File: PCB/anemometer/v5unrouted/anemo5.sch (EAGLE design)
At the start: 77 parts, among them IC1 AD8223, IC2 AD8223, IC3 AD8223, IC4 AD8223, IC5 TL072D, IC6 TL072D, IC7 TL072D, J1 RJ12STRAIGHT-I2C, J2 RJ12STRAIGHT-I2C

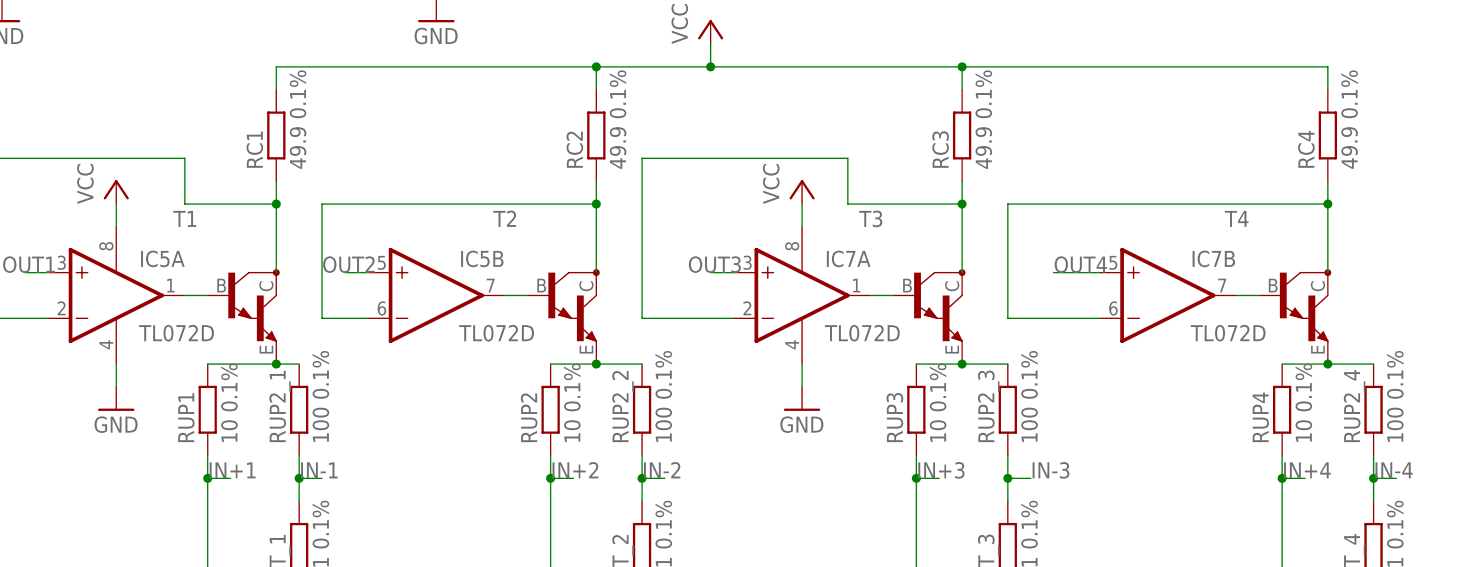
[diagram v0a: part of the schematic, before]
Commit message: changet to PNP darlington in unrouted anemometer file. should be rerouted if needed! (no changes in routed files...)
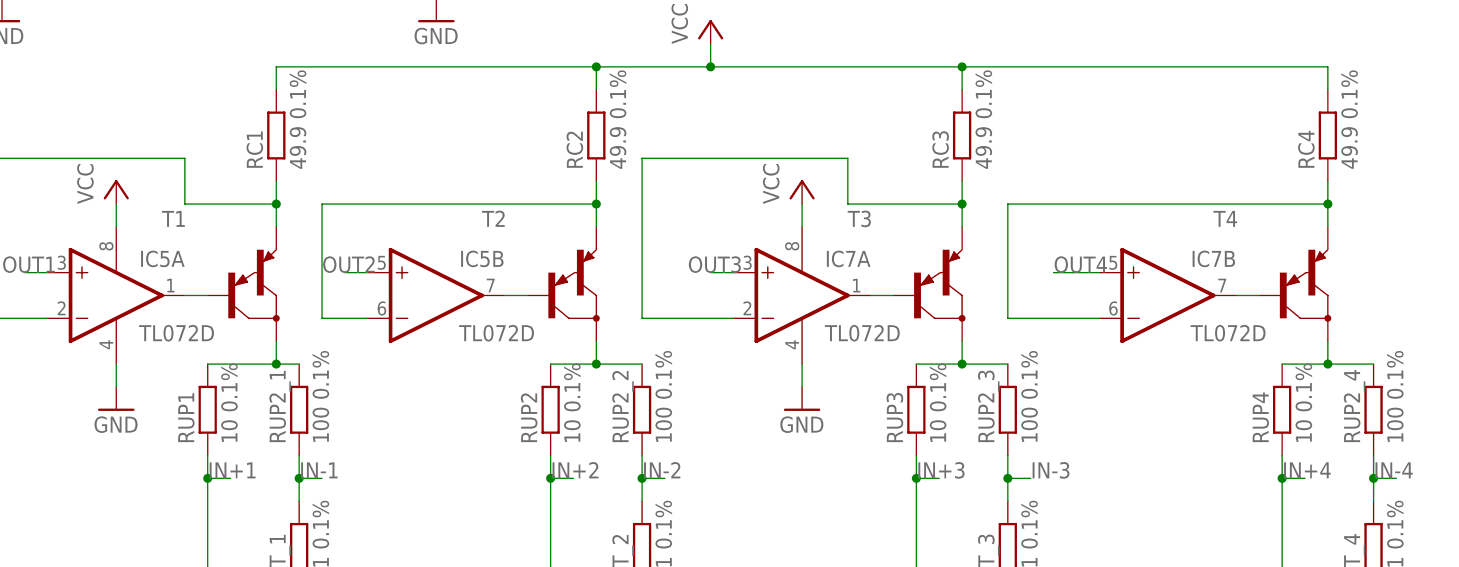
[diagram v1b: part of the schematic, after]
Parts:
- T1, T2, T3, T4: device transistor:MMBTA13LT1-NPN_DARL-SOT23-BEC -> transistor:MMBTA64LT1-PNP_DARL-SOT23-BEC
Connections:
- net N$11: now also T2.C; no longer T2.E
- net N$12: now also T3.C; no longer T3.E
- net N$13: now also T4.C; no longer T4.E
- net N$15: now also T1.E; no longer T1.C
- net N$16: now also T2.E; no longer T2.C
- net N$17: now also T3.E; no longer T3.C
- net N$22: now also T4.E; no longer T4.C
- net N$9: now also T1.C; no longer T1.E
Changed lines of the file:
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@@
 <part name="GND12" library="supply1" deviceset="GND" device=""/>
 <part name="GND13" library="supply1" deviceset="GND" device=""/>
-<part name="T1" library="transistor" deviceset="*-NPN_DARL-" device="SOT23-BEC" technology="MMBTA13LT1"/>
-<part name="T2" library="transistor" deviceset="*-NPN_DARL-" device="SOT23-BEC" technology="MMBTA13LT1"/>
-<part name="T3" library="transistor" deviceset="*-NPN_DARL-" device="SOT23-BEC" technology="MMBTA13LT1"/>
-<part name="T4" library="transistor" deviceset="*-NPN_DARL-" device="SOT23-BEC" technology="MMBTA13LT1"/>
 <part name="P+6" library="supply1" deviceset="VCC" device=""/>
 <part name="J1" library="lpatiny" deviceset="RJ12" device="STRAIGHT-I2C"/>
@@
 <part name="GND22" library="supply1" deviceset="GND" device=""/>
 <part name="C6" library="rcl" deviceset="C-EU" device="C1206" value="100n"/>
+<part name="T1" library="transistor" deviceset="*-PNP_DARL-" device="SOT23-BEC" technology="MMBTA64LT1"/>
+<part name="T2" library="transistor" deviceset="*-PNP_DARL-" device="SOT23-BEC" technology="MMBTA64LT1"/>
+<part name="T3" library="transistor" deviceset="*-PNP_DARL-" device="SOT23-BEC" technology="MMBTA64LT1"/>
+<part name="T4" library="transistor" deviceset="*-PNP_DARL-" device="SOT23-BEC" technology="MMBTA64LT1"/>
 </parts>
 <sheets>
@@
 <instance part="GND12" gate="1" x="104.14" y="33.02"/>
 <instance part="GND13" gate="1" x="152.4" y="33.02"/>
-<instance part="T1" gate="G$1" x="101.6" y="-7.62"/>
-<instance part="T2" gate="G$1" x="137.16" y="-7.62"/>
-<instance part="T3" gate="G$1" x="177.8" y="-7.62"/>
-<instance part="T4" gate="G$1" x="218.44" y="-7.62"/>
 <instance part="P+6" gate="VCC" x="154.94" y="22.86"/>
 <instance part="J1" gate="G$1" x="-25.4" y="-22.86" rot="R270"/>
@@
 <instance part="GND22" gate="1" x="60.96" y="-99.06"/>
 <instance part="C6" gate="G$1" x="66.04" y="-78.74" rot="R90"/>
+<instance part="T1" gate="G$1" x="101.6" y="-7.62"/>
+<instance part="T2" gate="G$1" x="137.16" y="-7.62"/>
+<instance part="T3" gate="G$1" x="177.8" y="-7.62"/>
+<instance part="T4" gate="G$1" x="218.44" y="-7.62"/>
 </instances>
 <busses>
@@
 <pinref part="RUP2_1" gate="G$1" pin="2"/>
 <wire x1="99.06" y1="-15.24" x2="106.68" y2="-15.24" width="0.1524" layer="91"/>
-<pinref part="T1" gate="G$1" pin="E"/>
+<pinref part="T1" gate="G$1" pin="C"/>
 <wire x1="106.68" y1="-15.24" x2="109.22" y2="-15.24" width="0.1524" layer="91"/>
+<wire x1="106.68" y1="-12.7" x2="106.68" y2="-15.24" width="0.1524" layer="91"/>
 <junction x="106.68" y="-15.24"/>
 </segment>
@@
 <pinref part="RUP2_2" gate="G$1" pin="2"/>
 <wire x1="137.16" y1="-15.24" x2="142.24" y2="-15.24" width="0.1524" layer="91"/>
-<pinref part="T2" gate="G$1" pin="E"/>
+<pinref part="T2" gate="G$1" pin="C"/>
 <wire x1="142.24" y1="-15.24" x2="147.32" y2="-15.24" width="0.1524" layer="91"/>
+<wire x1="142.24" y1="-12.7" x2="142.24" y2="-15.24" width="0.1524" layer="91"/>
 <junction x="142.24" y="-15.24"/>
 </segment>
@@
 <pinref part="RUP2_3" gate="G$1" pin="2"/>
 <wire x1="177.8" y1="-15.24" x2="182.88" y2="-15.24" width="0.1524" layer="91"/>
-<pinref part="T3" gate="G$1" pin="E"/>
+<pinref part="T3" gate="G$1" pin="C"/>
 <wire x1="182.88" y1="-15.24" x2="187.96" y2="-15.24" width="0.1524" layer="91"/>
+<wire x1="182.88" y1="-12.7" x2="182.88" y2="-15.24" width="0.1524" layer="91"/>
 <junction x="182.88" y="-15.24"/>
 </segment>
@@
 <pinref part="RUP2_4" gate="G$1" pin="2"/>
 <wire x1="218.44" y1="-15.24" x2="223.52" y2="-15.24" width="0.1524" layer="91"/>
-<pinref part="T4" gate="G$1" pin="E"/>
+<pinref part="T4" gate="G$1" pin="C"/>
 <wire x1="223.52" y1="-15.24" x2="228.6" y2="-15.24" width="0.1524" layer="91"/>
+<wire x1="223.52" y1="-12.7" x2="223.52" y2="-15.24" width="0.1524" layer="91"/>
 <junction x="223.52" y="-15.24"/>
 </segment>
@@
 <net name="OUT1A" class="0">
 <segment>
-<pinref part="T1" gate="G$1" pin="B"/>
 <wire x1="99.06" y1="-7.62" x2="96.52" y2="-7.62" width="0.1524" layer="91"/>
 <pinref part="IC5" gate="A" pin="OUT"/>
+<pinref part="T1" gate="G$1" pin="B"/>
 </segment>
 </net>
 <net name="OUT2A" class="0">
 <segment>
-<pinref part="T2" gate="G$1" pin="B"/>
 <wire x1="134.62" y1="-7.62" x2="132.08" y2="-7.62" width="0.1524" layer="91"/>
 <pinref part="IC5" gate="B" pin="OUT"/>
+<pinref part="T2" gate="G$1" pin="B"/>
 </segment>
 </net>
 <net name="OUT3A" class="0">
 <segment>
-<pinref part="T3" gate="G$1" pin="B"/>
 <wire x1="175.26" y1="-7.62" x2="172.72" y2="-7.62" width="0.1524" layer="91"/>
 <pinref part="IC7" gate="A" pin="OUT"/>
+<pinref part="T3" gate="G$1" pin="B"/>
 </segment>
 </net>
 <net name="OUT4A" class="0">
 <segment>
-<pinref part="T4" gate="G$1" pin="B"/>
 <wire x1="215.9" y1="-7.62" x2="213.36" y2="-7.62" width="0.1524" layer="91"/>
 <pinref part="IC7" gate="B" pin="OUT"/>
+<pinref part="T4" gate="G$1" pin="B"/>
 </segment>
 </net>
 <net name="N$15" class="2">
 <segment>
-<pinref part="T1" gate="G$1" pin="C"/>
-<wire x1="106.68" y1="2.54" x2="106.68" y2="-5.08" width="0.1524" layer="91"/>
+<wire x1="106.68" y1="2.54" x2="106.68" y2="0" width="0.1524" layer="91"/>
 <wire x1="96.52" y1="2.54" x2="106.68" y2="2.54" width="0.1524" layer="91"/>
 <wire x1="96.52" y1="7.62" x2="96.52" y2="2.54" width="0.1524" layer="91"/>
@@
 <wire x1="106.68" y1="5.08" x2="106.68" y2="2.54" width="0.1524" layer="91"/>
 <junction x="106.68" y="2.54"/>
+<pinref part="T1" gate="G$1" pin="E"/>
 </segment>
 </net>
 <net name="N$16" class="2">
 <segment>
-<pinref part="T2" gate="G$1" pin="C"/>
-<wire x1="142.24" y1="-5.08" x2="142.24" y2="2.54" width="0.1524" layer="91"/>
+<wire x1="142.24" y1="0" x2="142.24" y2="2.54" width="0.1524" layer="91"/>
 <wire x1="111.76" y1="2.54" x2="142.24" y2="2.54" width="0.1524" layer="91"/>
 <pinref part="IC5" gate="B" pin="-IN"/>
@@
 <wire x1="142.24" y1="5.08" x2="142.24" y2="2.54" width="0.1524" layer="91"/>
 <junction x="142.24" y="2.54"/>
+<pinref part="T2" gate="G$1" pin="E"/>
 </segment>
 </net>
 <net name="N$17" class="2">
 <segment>
-<pinref part="T3" gate="G$1" pin="C"/>
-<wire x1="182.88" y1="2.54" x2="182.88" y2="-5.08" width="0.1524" layer="91"/>
+<wire x1="182.88" y1="2.54" x2="182.88" y2="0" width="0.1524" layer="91"/>
 <wire x1="170.18" y1="2.54" x2="182.88" y2="2.54" width="0.1524" layer="91"/>
 <wire x1="170.18" y1="7.62" x2="170.18" y2="2.54" width="0.1524" layer="91"/>
@@
 <wire x1="182.88" y1="5.08" x2="182.88" y2="2.54" width="0.1524" layer="91"/>
 <junction x="182.88" y="2.54"/>
+<pinref part="T3" gate="G$1" pin="E"/>
 </segment>
 </net>
 <net name="N$22" class="2">
 <segment>
-<pinref part="T4" gate="G$1" pin="C"/>
-<wire x1="223.52" y1="2.54" x2="223.52" y2="-5.08" width="0.1524" layer="91"/>
+<wire x1="223.52" y1="2.54" x2="223.52" y2="0" width="0.1524" layer="91"/>
 <wire x1="187.96" y1="2.54" x2="223.52" y2="2.54" width="0.1524" layer="91"/>
 <pinref part="IC7" gate="B" pin="-IN"/>
@@
 <wire x1="223.52" y1="2.54" x2="223.52" y2="5.08" width="0.1524" layer="91"/>
 <junction x="223.52" y="2.54"/>
-</segment>
-</net>
+<pinref part="T4" gate="G$1" pin="E"/>
+</segment>
+</net>
